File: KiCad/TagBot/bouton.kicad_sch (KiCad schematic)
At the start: 5 parts, among them U501 BU33SD5WG-TR

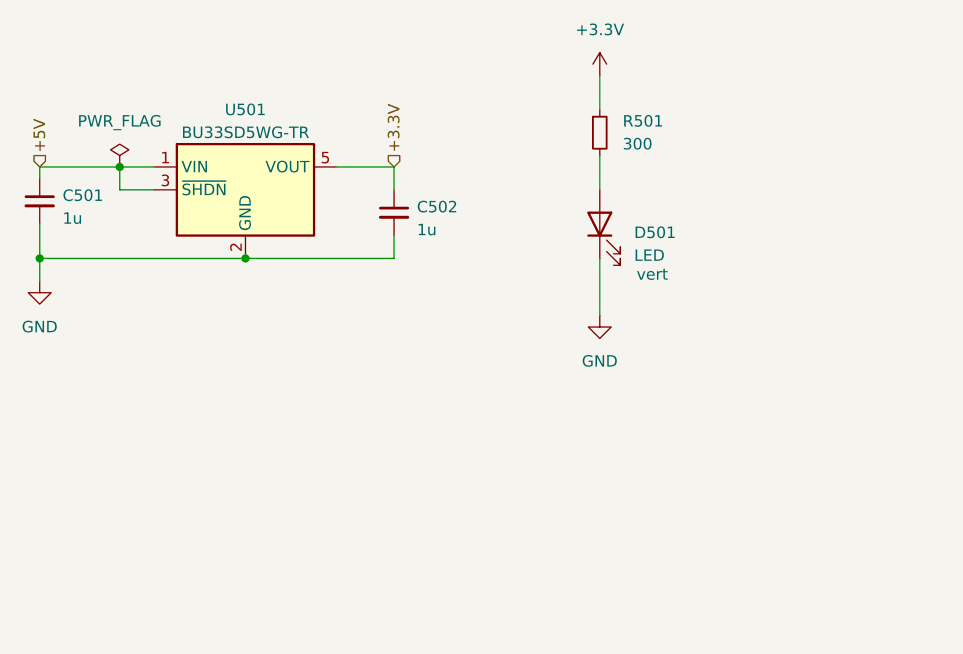
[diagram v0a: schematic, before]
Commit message: correction schema kicad
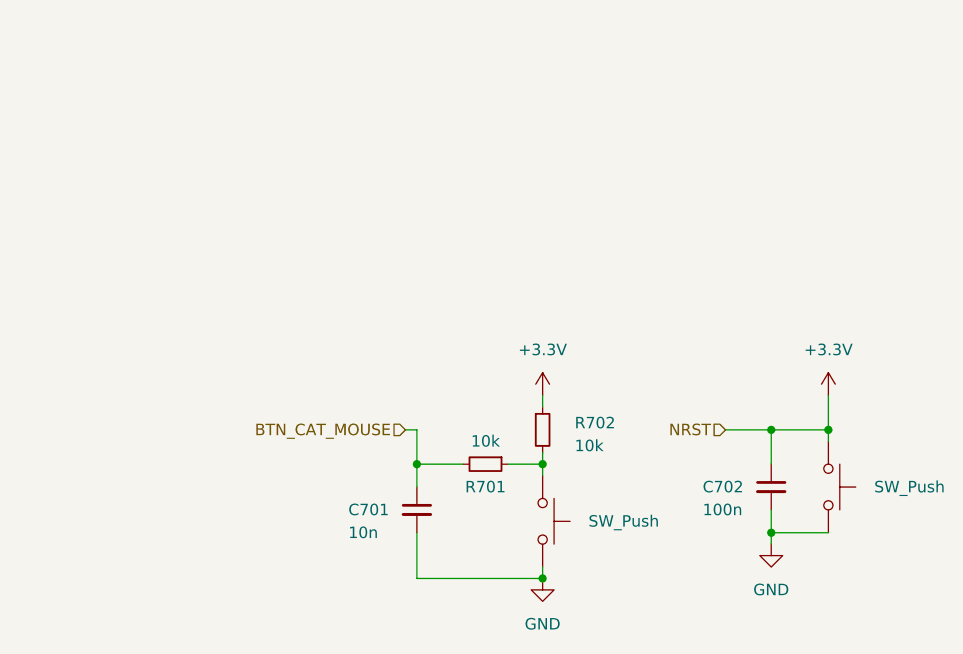
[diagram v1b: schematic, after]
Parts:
- removed C501, C502: 1u, Capacitor_SMD:C_0402_1005Metric, symbol Device:C_Small
- removed D501: LED, LED_SMD:LED_0603_1608Metric, symbol Device:LED
- removed R501: 300, Resistor_SMD:R_0402_1005Metric, symbol Device:R_Small
- removed U501: BU33SD5WG-TR, Package_TO_SOT_SMD:SOT-23-5, symbol Regulator_Linear:MCP1802x-xx02xOT
- added C701: 10n, Capacitor_SMD:C_0402_1005Metric, symbol Device:C_Small
- added C702: 100n, Capacitor_SMD:C_0402_1005Metric, symbol Device:C_Small
- added R701, R702: 10k, Resistor_SMD:R_0402_1005Metric, symbol Device:R_Small
- added SW701, SW702: SW_Push, Button_Switch_SMD:SW_Push_1P1T_NO_6x6mm_H9.5mm, symbol Switch:SW_Push
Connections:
- net +3.3V: now also C702.1, R702.1, SW702.1
- net GND: now also C701.2, C702.2, SW701.2, SW702.2
- new net: R701.1, R702.2, SW701.1
- new net BTN_CAT_MOUSE: C701.1, R701.2

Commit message: placement pcb 2
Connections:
- net +3.3V: no longer C702.1, SW702.1
- new net NRST: C702.1, SW702.1
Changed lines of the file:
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@@
-	)
-	(junction
-		(at 223.52 129.54)
-		(diameter 0)
-		(color 0 0 0 0)
 	)
 	(junction
@@
 		(pts
 			(xy 187.96 133.35) (xy 191.77 133.35)
-		)
-		(stroke
-			(width 0)
-			(type default)
-		)
-	)
-	(wire
-		(pts
-			(xy 223.52 125.73) (xy 223.52 129.54)
 		)
 		(stroke
@@
 					(unit 1)
 				)
-			)
-		)
-	)
-	(symbol
-		(lib_name "+3.3V_2")
-		(lib_id "power:+3.3V")
-		(at 223.52 125.73 0)
-		(unit 1)
-		(exclude_from_sim no)
-		(in_bom yes)
-		(on_board yes)
-		(dnp no)
-		(fields_autoplaced yes)
-		(property "Reference" "#PWR0704"
-			(at 223.52 129.54 0)
-			(effects
-				(font
-					(size 1.27 1.27)
-				)
-				(hide yes)
-			)
-		)
-		(property "Value" "+3.3V"
-			(at 223.52 120.65 0)
-			(effects
-				(font
-					(size 1.27 1.27)
-				)
-			)
-		)
-		(property "Footprint" ""
-			(at 223.52 125.73 0)
-			(effects
-				(font
-					(size 1.27 1.27)
-				)
-				(hide yes)
-			)
-		)
-		(property "Datasheet" ""
-			(at 223.52 125.73 0)
-			(effects
-				(font
-					(size 1.27 1.27)
-				)
-				(hide yes)
-			)
-		)
-		(property "Description" "Power symbol creates a global label with name \"+3.3V\""
-			(at 223.52 125.73 0)
-			(effects
-				(font
-					(size 1.27 1.27)
-				)
-				(hide yes)
-			)
-		)
-		(pin "1"
-		)
-		(instances
-			(project "TagBot"
-				(path "/6db08f37-7cb3-4000-93f1-ba0d0ffbeb19/749bc4ce-f5ad-49bc-96d6-41722e423715"
-					(reference "#PWR0704")
-					(unit 1)
-				)
